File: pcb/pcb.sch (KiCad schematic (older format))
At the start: 14 parts, among them J1 Raspberry_Pi_2_3

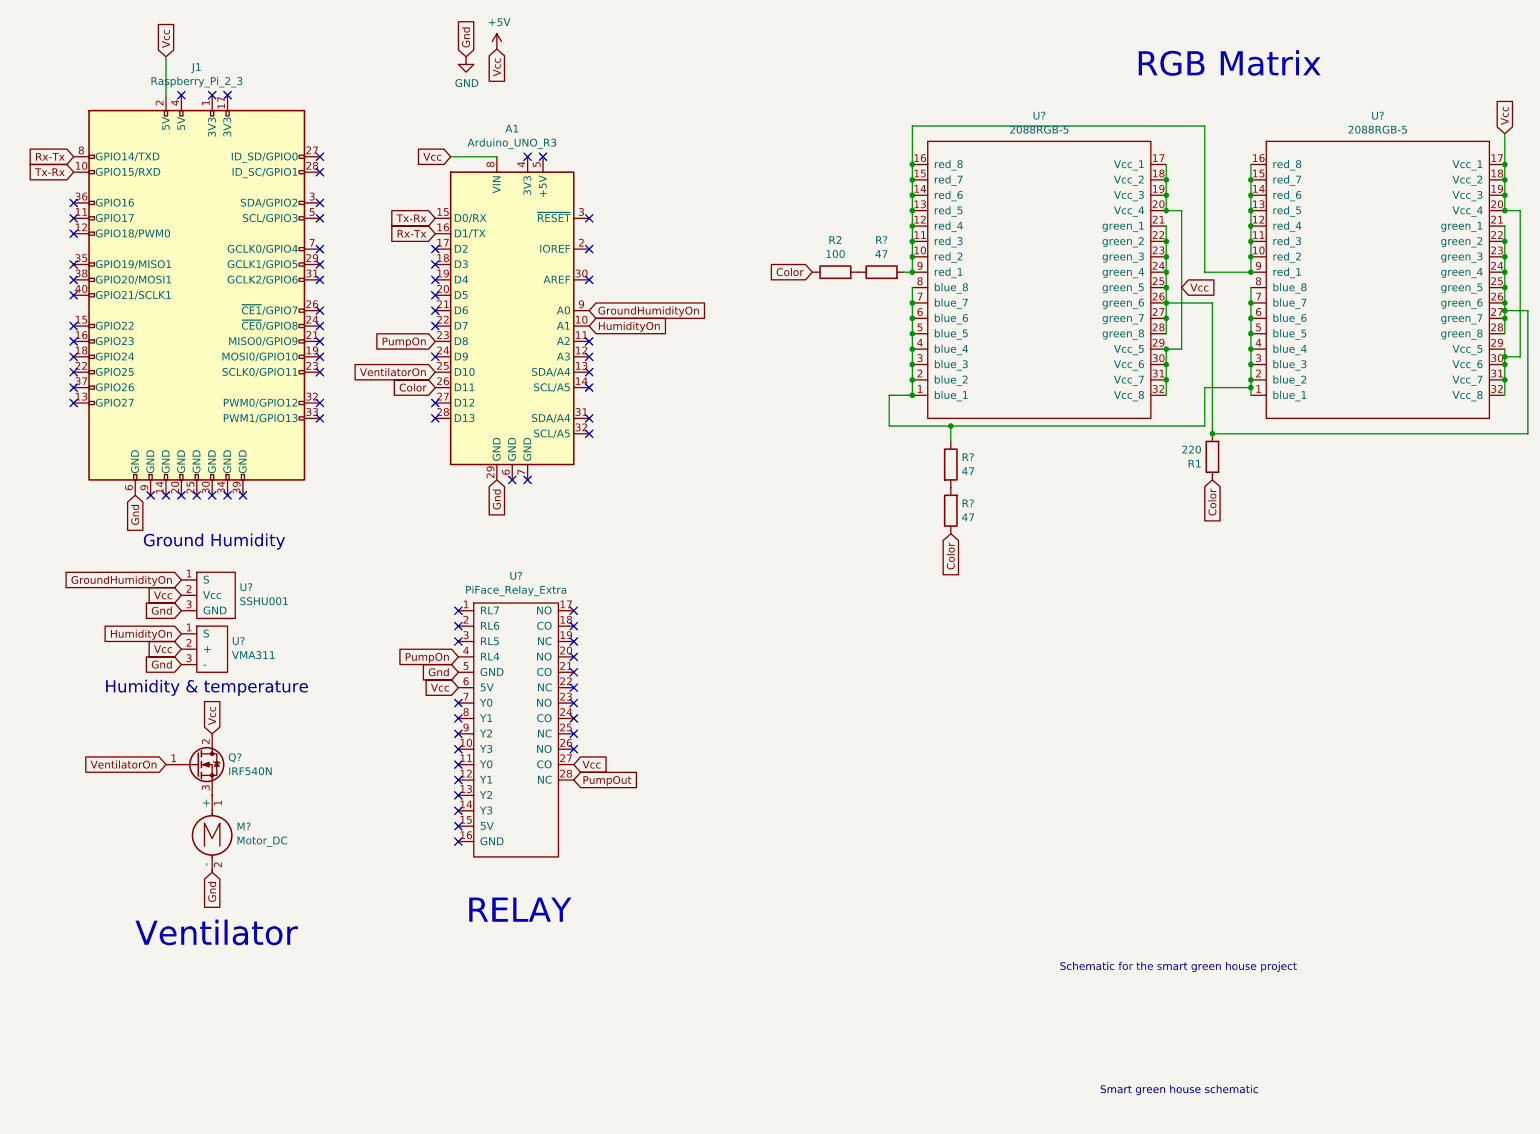
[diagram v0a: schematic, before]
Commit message: change labels name
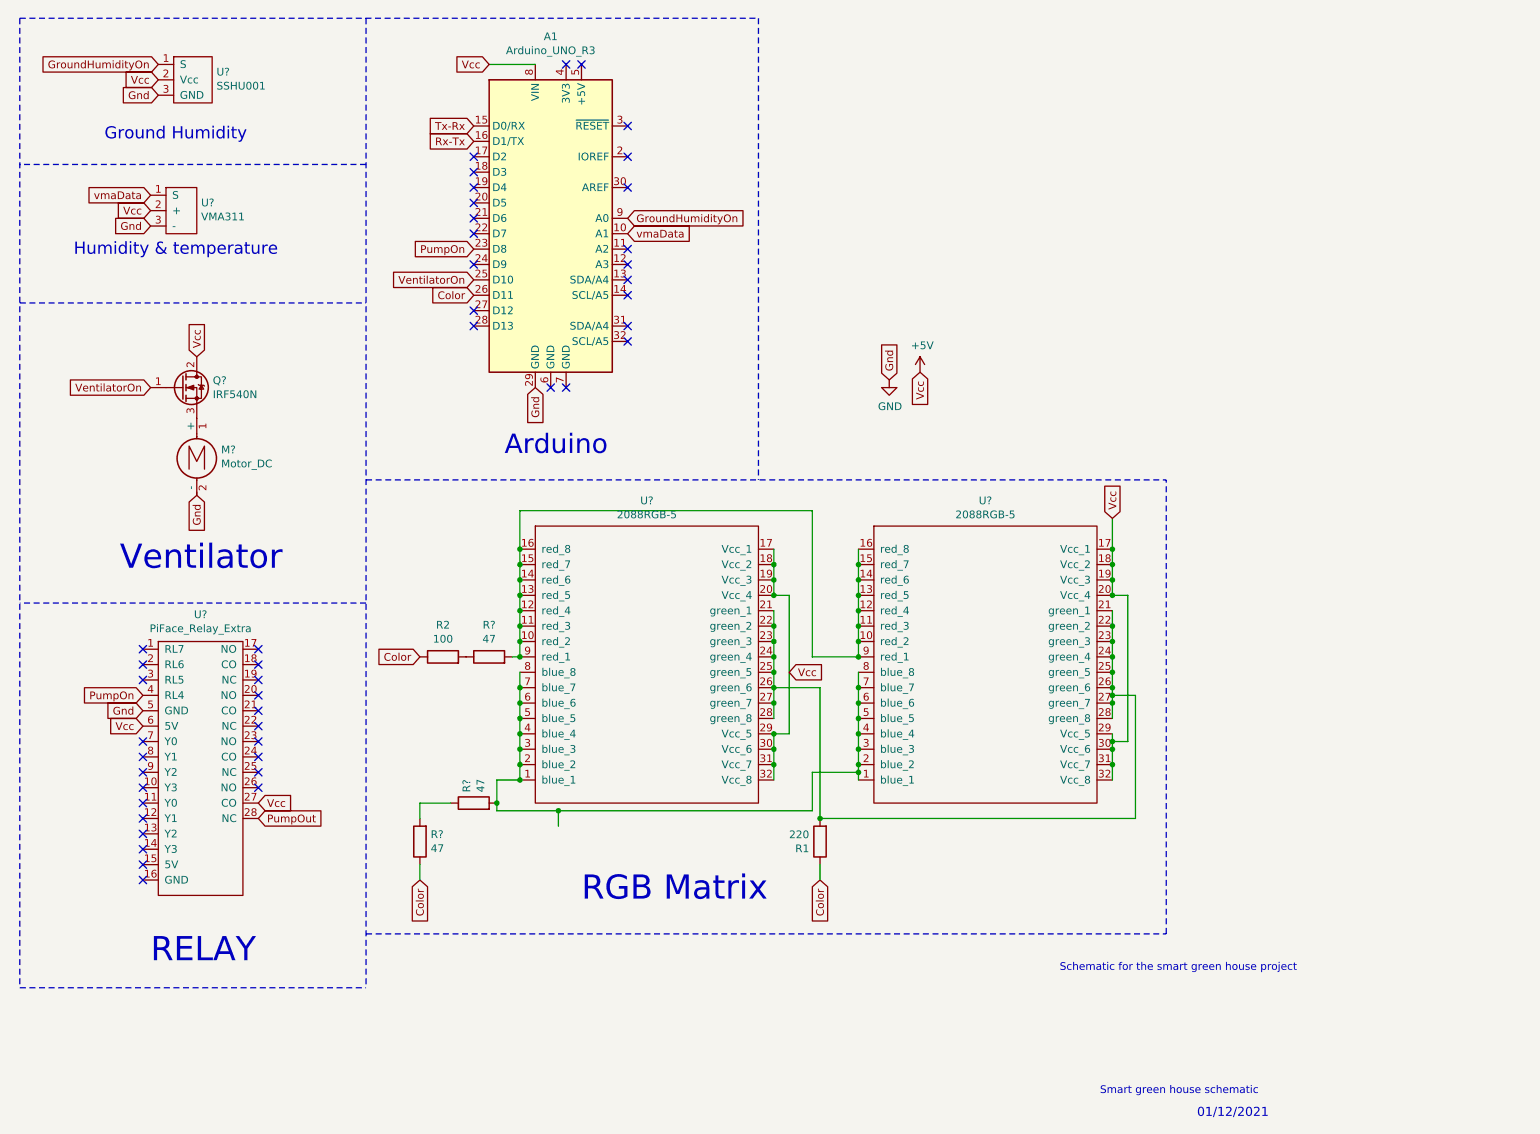
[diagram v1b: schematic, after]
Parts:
- removed J1: Raspberry_Pi_2_3, symbol Connector:Raspberry_Pi_2_3
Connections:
- net at U?.1 (blue_1), U?.1 (blue_1), U?.2 (blue_2)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: now also R?.2; no longer R?.1
- net at R?.2: now also R?.1; no longer R?.2
- net HumidityOn renamed vmaData
- no-connect marks 81 -> 45
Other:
- note added: "01/12/2021"
- note added: "Arduino"
- moved on the sheet: A1, M?, Q?, R1, R2, R?, U?
